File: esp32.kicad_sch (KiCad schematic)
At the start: 2 parts, among them U11 T-Display-S3

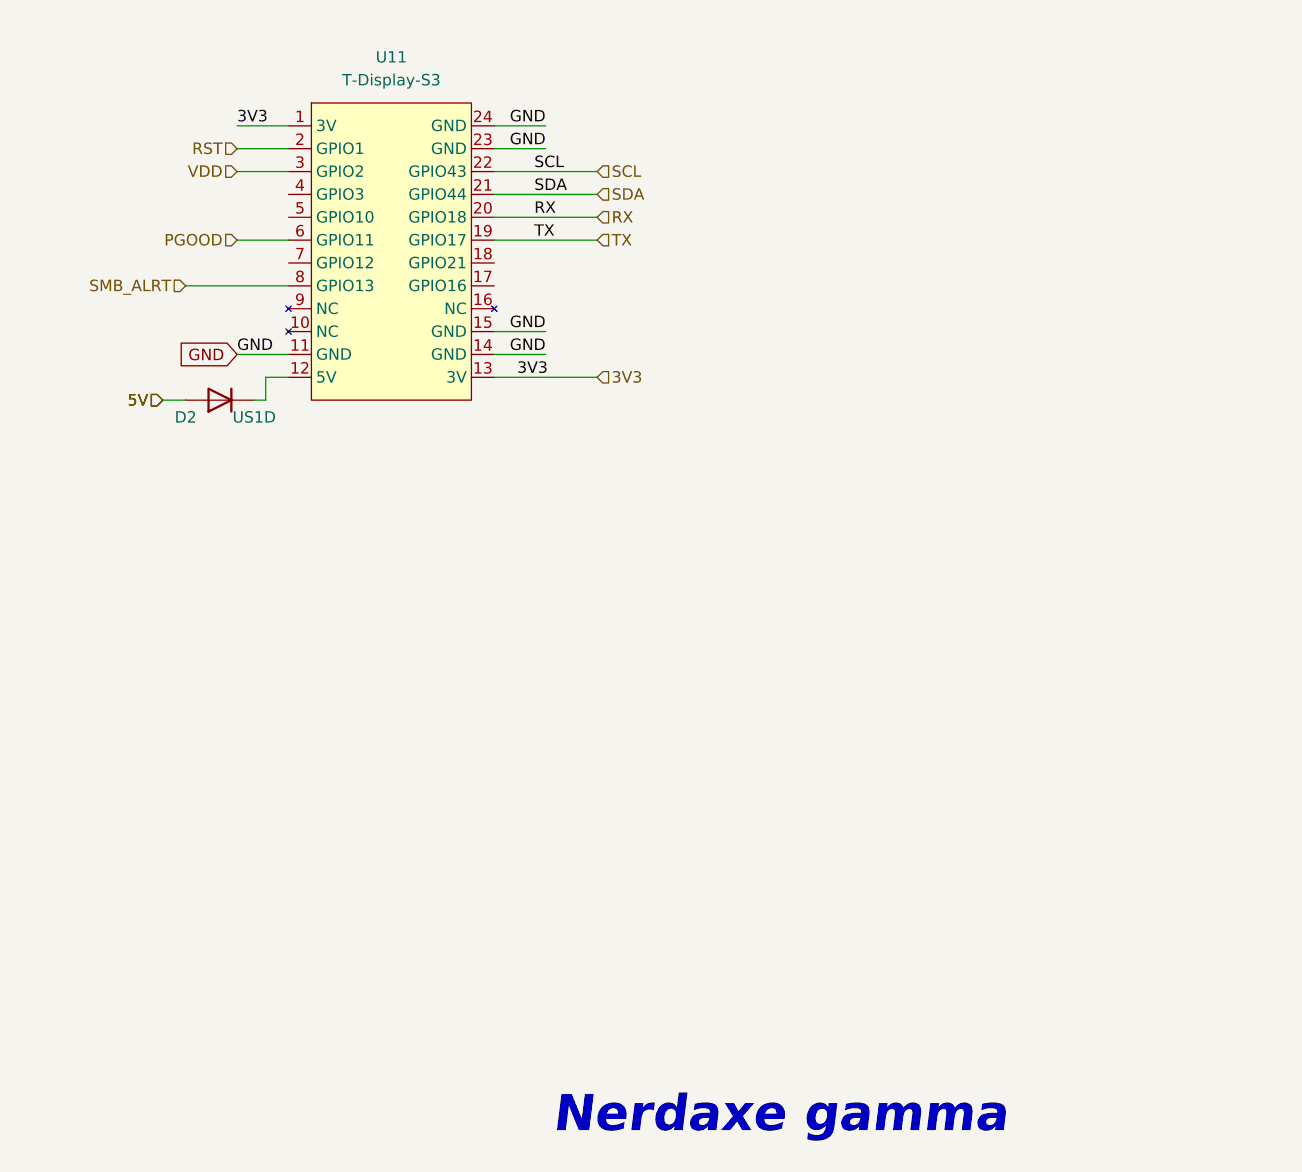
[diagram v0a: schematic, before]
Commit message: Nerdaxe Gamma v2.3
- Fix Emi CE needs
- Added ferrite beads + EMI blocking capacitors
- New components added: R16, R20, R26, R27C21, C22, C23, FB1, FB2, FB3, FB4, FB5, FB6
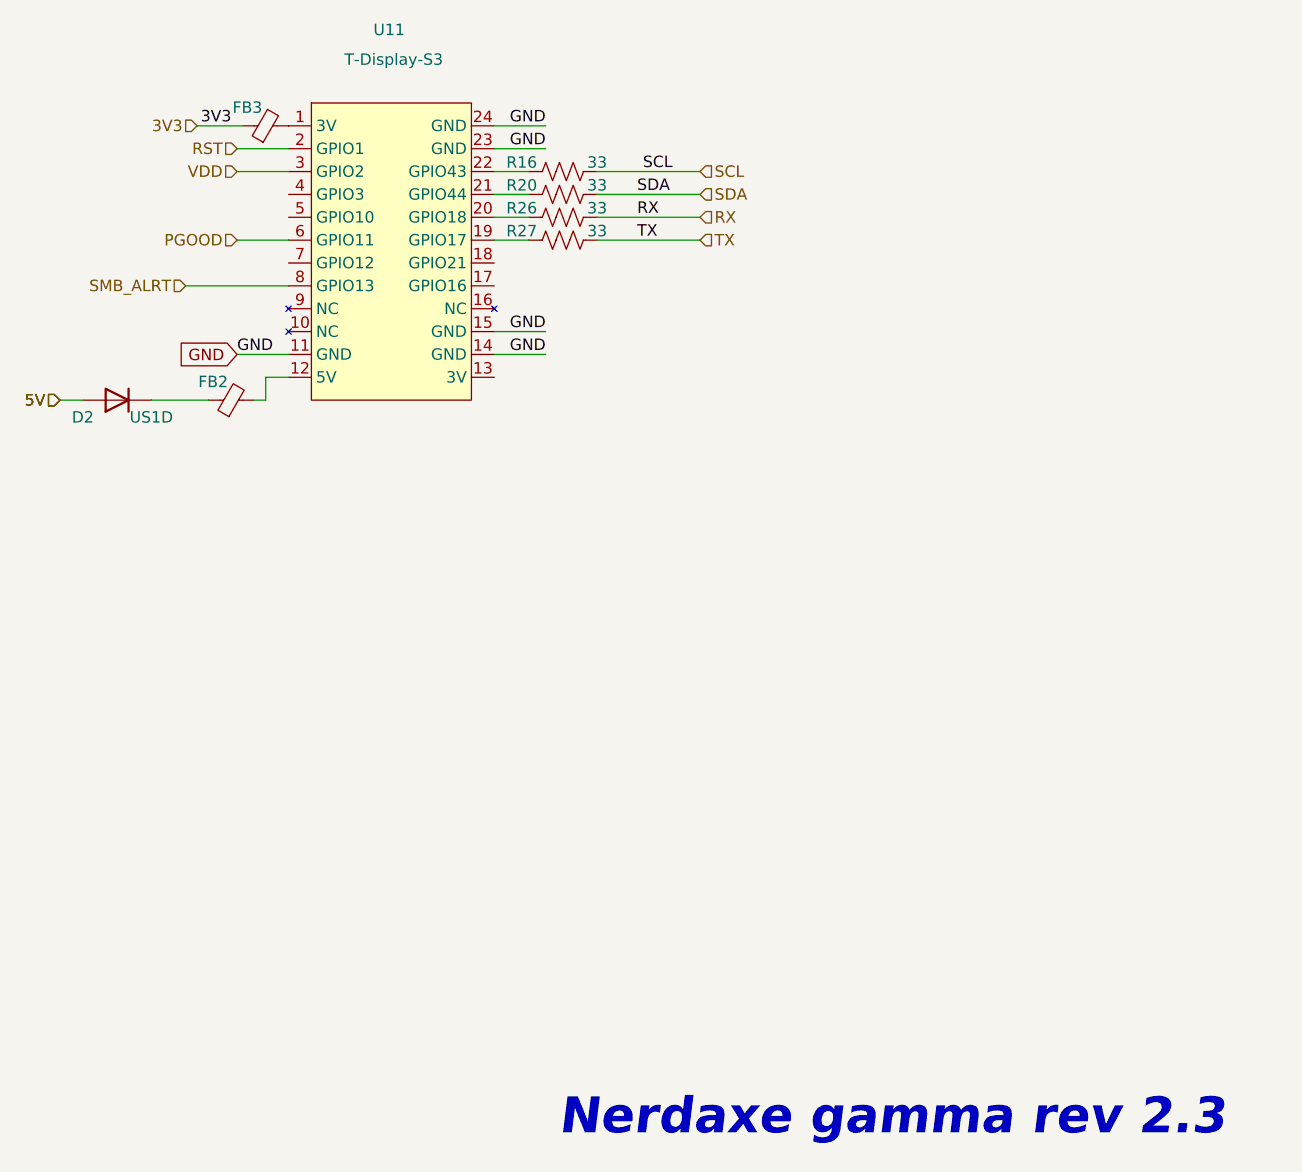
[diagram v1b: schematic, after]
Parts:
- added FB2: MPZ2012S221A, Resistor_SMD:R_0805_2012Metric, symbol Device:FerriteBead_Small
- added FB3: BLM21PG221SN1D, Resistor_SMD:R_0805_2012Metric, symbol Device:FerriteBead_Small
- added R16, R20, R26, R27: 33, Resistor_SMD:R_0805_2012Metric, symbol Device:R_US
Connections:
- net 3V3: now also FB3.1; no longer U11.1 (3V), U11.13 (3V)
- net RX: now also R26.2; no longer U11.20 (GPIO18)
- net SCL: now also R16.2; no longer U11.22 (GPIO43)
- net SDA: now also R20.2; no longer U11.21 (GPIO44)
- net TX: now also R27.2; no longer U11.19 (GPIO17)
- net at D2.1 (K): now also FB2.1; no longer U11.12 (5V)
- new net: R27.1, U11.19 (GPIO17)
- new net: FB3.2, U11.1 (3V)
- new net: FB2.2, U11.12 (5V)
- new net: R26.1, U11.20 (GPIO18)
- new net: R16.1, U11.22 (GPIO43)
- new net: R20.1, U11.21 (GPIO44)
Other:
- note added: "Nerdaxe gamma rev 2.3"
- note removed: "Nerdaxe gamma"
- moved on the sheet: D2
